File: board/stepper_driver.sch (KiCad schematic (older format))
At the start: 28 parts, among them J2301 CONN_STEPPER, J2302 CONN_2, U2301 L6470

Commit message: Worked a little on the PCB layout.
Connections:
- net at C2301.1, D2301.3 (cathode), U2301.14 (VBOOT): no longer C2302.1
- net at C2302.2, U2301.13 (CP): no longer D2301.2 (AK)
- new net: C2302.1, D2301.2 (AK)
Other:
- moved on the sheet: C2401, C2402, D2401
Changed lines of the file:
@@
 L +24V #PWR0185
 U 1 1 52E46E92
-P 6150 2000
+P 6000 2000
 AR Path="/52E6C2E8/52E46E92" Ref="#PWR0185"  Part="1"
 AR Path="/52FD6269/52E46E92" Ref="#PWR0216"  Part="1"
 AR Path="/52FD745B/52E46E92" Ref="#PWR0247"  Part="1"
 AR Path="/52FD7E0D/52E46E92" Ref="#PWR0278"  Part="1"
-F 0 "#PWR0216" H 6150 1950 20  0001 C CNN
-F 1 "+24V" H 6150 2100 30  0000 C CNN
-F 2 "" H 6150 2000 60  0000 C CNN
-F 3 "" H 6150 2000 60  0000 C CNN
-	1    6150 2000
+F 0 "#PWR0216" H 6000 1950 20  0001 C CNN
+F 1 "+24V" H 6000 2100 30  0000 C CNN
+F 2 "" H 6000 2000 60  0000 C CNN
+F 3 "" H 6000 2000 60  0000 C CNN
+	1    6000 2000
 	1    0    0    -1
 $EndComp
@@
 Text HLabel 4350 4750 0    60   Input ~ 0
 SCK
-Text HLabel 4350 4850 0    60   Input ~ 0
+Text HLabel 4350 4850 0    60   Output ~ 0
 SDO
 Text HLabel 4350 4950 0    60   Input ~ 0
@@
 L C C2301
 U 1 1 52E47AD8
-P 5700 2100
+P 5550 2100
 AR Path="/52E6C2E8/52E47AD8" Ref="C2301"  Part="1"
 AR Path="/52FD6269/52E47AD8" Ref="C2401"  Part="1"
 AR Path="/52FD745B/52E47AD8" Ref="C2501"  Part="1"
 AR Path="/52FD7E0D/52E47AD8" Ref="C2601"  Part="1"
-F 0 "C2401" H 5700 2200 40  0000 L CNN
-F 1 "220nF" H 5706 2015 40  0000 L CNN
-F 2 "" H 5738 1950 30  0000 C CNN
-F 3 "http://www.digikey.ca/product-detail/en/CL21B224KCFSFNE/1276-2949-1-ND/3891035" H 5700 2100 60  0001 C CNN
-F 4 "1276-2949-1-ND" H 6900 4550 60  0001 C CNN "Digikey Number"
-	1    5700 2100
+F 0 "C2401" H 5550 2200 40  0000 L CNN
+F 1 "220nF" H 5556 2015 40  0000 L CNN
+F 2 "" H 5588 1950 30  0000 C CNN
+F 3 "http://www.digikey.ca/product-detail/en/CL21B224KCFSFNE/1276-2949-1-ND/3891035" H 5550 2100 60  0001 C CNN
+F 4 "1276-2949-1-ND" H 6750 4550 60  0001 C CNN "Digikey Number"
+	1    5550 2100
 	0    -1   -1   0
 $EndComp
@@
 L C C2302
 U 1 1 52E47AE3
-P 5450 2700
+P 5550 2850
 AR Path="/52E6C2E8/52E47AE3" Ref="C2302"  Part="1"
 AR Path="/52FD6269/52E47AE3" Ref="C2402"  Part="1"
 AR Path="/52FD745B/52E47AE3" Ref="C2502"  Part="1"
 AR Path="/52FD7E0D/52E47AE3" Ref="C2602"  Part="1"
-F 0 "C2402" H 5450 2800 40  0000 L CNN
-F 1 "10nF" H 5456 2615 40  0000 L CNN
-F 2 "" H 5488 2550 30  0000 C CNN
-F 3 "http://www.digikey.ca/product-detail/en/C1608X7R2A103K080AA/445-1304-1-ND/567706" H 5450 2700 60  0001 C CNN
-F 4 "445-1304-1-ND" H 6900 4550 60  0001 C CNN "Digikey Number"
-	1    5450 2700
-	0    -1   -1   0
+F 0 "C2402" H 5550 2950 40  0000 L CNN
+F 1 "10nF" H 5556 2765 40  0000 L CNN
+F 2 "" H 5588 2700 30  0000 C CNN
+F 3 "http://www.digikey.ca/product-detail/en/C1608X7R2A103K080AA/445-1304-1-ND/567706" H 5550 2850 60  0001 C CNN
+F 4 "445-1304-1-ND" H 7000 4700 60  0001 C CNN "Digikey Number"
+	1    5550 2850
+	1    0    0    -1
 $EndComp
 $Comp
 L DOUBLE_SCHOTTKY D2301
 U 1 1 52F6EE9F
-P 5700 2350
+P 5550 2350
 AR Path="/52E6C2E8/52F6EE9F" Ref="D2301"  Part="1"
 AR Path="/52FD6269/52F6EE9F" Ref="D2401"  Part="1"
 AR Path="/52FD745B/52F6EE9F" Ref="D2501"  Part="1"
 AR Path="/52FD7E0D/52F6EE9F" Ref="D2601"  Part="1"
-F 0 "D2401" H 5800 2250 40  0000 C CNN
-F 1 "DOUBLE_SCHOTTKY" H 5700 2450 40  0001 C CNN
-F 2 "" H 5700 2350 60  0000 C CNN
-F 3 "http://www.digikey.ca/product-detail/en/BAS70-04-TP/BAS70-04TPMSCT-ND/717333" H 5700 2350 60  0001 C CNN
-F 4 "BAS70-04TPMSCT-ND" H 6900 4550 60  0001 C CNN "Digikey Number"
-	1    5700 2350
+F 0 "D2401" H 5650 2250 40  0000 C CNN
+F 1 "DOUBLE_SCHOTTKY" H 5550 2450 40  0001 C CNN
+F 2 "" H 5550 2350 60  0000 C CNN
+F 3 "http://www.digikey.ca/product-detail/en/BAS70-04-TP/BAS70-04TPMSCT-ND/717333" H 5550 2350 60  0001 C CNN
+F 4 "BAS70-04TPMSCT-ND" H 6750 4550 60  0001 C CNN "Digikey Number"
+	1    5550 2350
 	-1   0    0    -1
 $EndComp
@@
 	1    0    0    -1
 $EndComp
-Text HLabel 1800 4450 0    60   BiDi ~ 0
+Text HLabel 1800 4450 0    60   Input ~ 0
 ~STBY/RST
 $Comp
@@
 Text Notes 6700 2400 0    60   ~ 0
 1 per Corner
-Text Notes 5350 1800 0    60   ~ 0
+Text Notes 5200 1800 0    60   ~ 0
 Charge Pump
 Wire Wire Line
@@
 Connection ~ 5750 3250
 Wire Wire Line
-	5200 2700 5250 2700
-Wire Wire Line
-	5300 2350 5200 2350
-Connection ~ 5200 2350
-Connection ~ 5200 2700
-Connection ~ 6150 2100
-Wire Wire Line
-	6150 2350 6100 2350
-Wire Wire Line
-	6150 2000 6150 2350
-Wire Wire Line
-	5900 2100 6150 2100
-Wire Wire Line
-	5200 2100 5200 2950
-Wire Wire Line
-	5200 2100 5500 2100
-Wire Wire Line
-	5450 2950 5450 3350
-Wire Wire Line
-	5550 2950 5550 3350
+	5150 2350 5050 2350
+Connection ~ 5050 2350
+Connection ~ 6000 2100
+Wire Wire Line
+	6000 2350 5950 2350
+Wire Wire Line
+	6000 2000 6000 2350
+Wire Wire Line
+	5750 2100 6000 2100
+Wire Wire Line
+	5050 2100 5350 2100
 Wire Wire Line
 	5450 5750 5450 5850
@@
 Wire Wire Line
 	3850 3100 3850 3200
-Wire Wire Line
-	5700 2550 5700 2950
-Wire Wire Line
-	5650 2700 5700 2700
-Connection ~ 5700 2700
-Wire Wire Line
-	5200 2950 5450 2950
-Wire Wire Line
-	5700 2950 5550 2950
 Wire Wire Line
 	6550 3850 6650 3850
@@
 	1    0    0    -1
 $EndComp
+Wire Wire Line
+	5050 2100 5050 3000
+Wire Wire Line
+	5050 3000 5450 3000
+Wire Wire Line
+	5450 3000 5450 3350
+Wire Wire Line
+	5550 3350 5550 3050
+Wire Wire Line
+	5550 2650 5550 2550
 $EndSCHEMATC

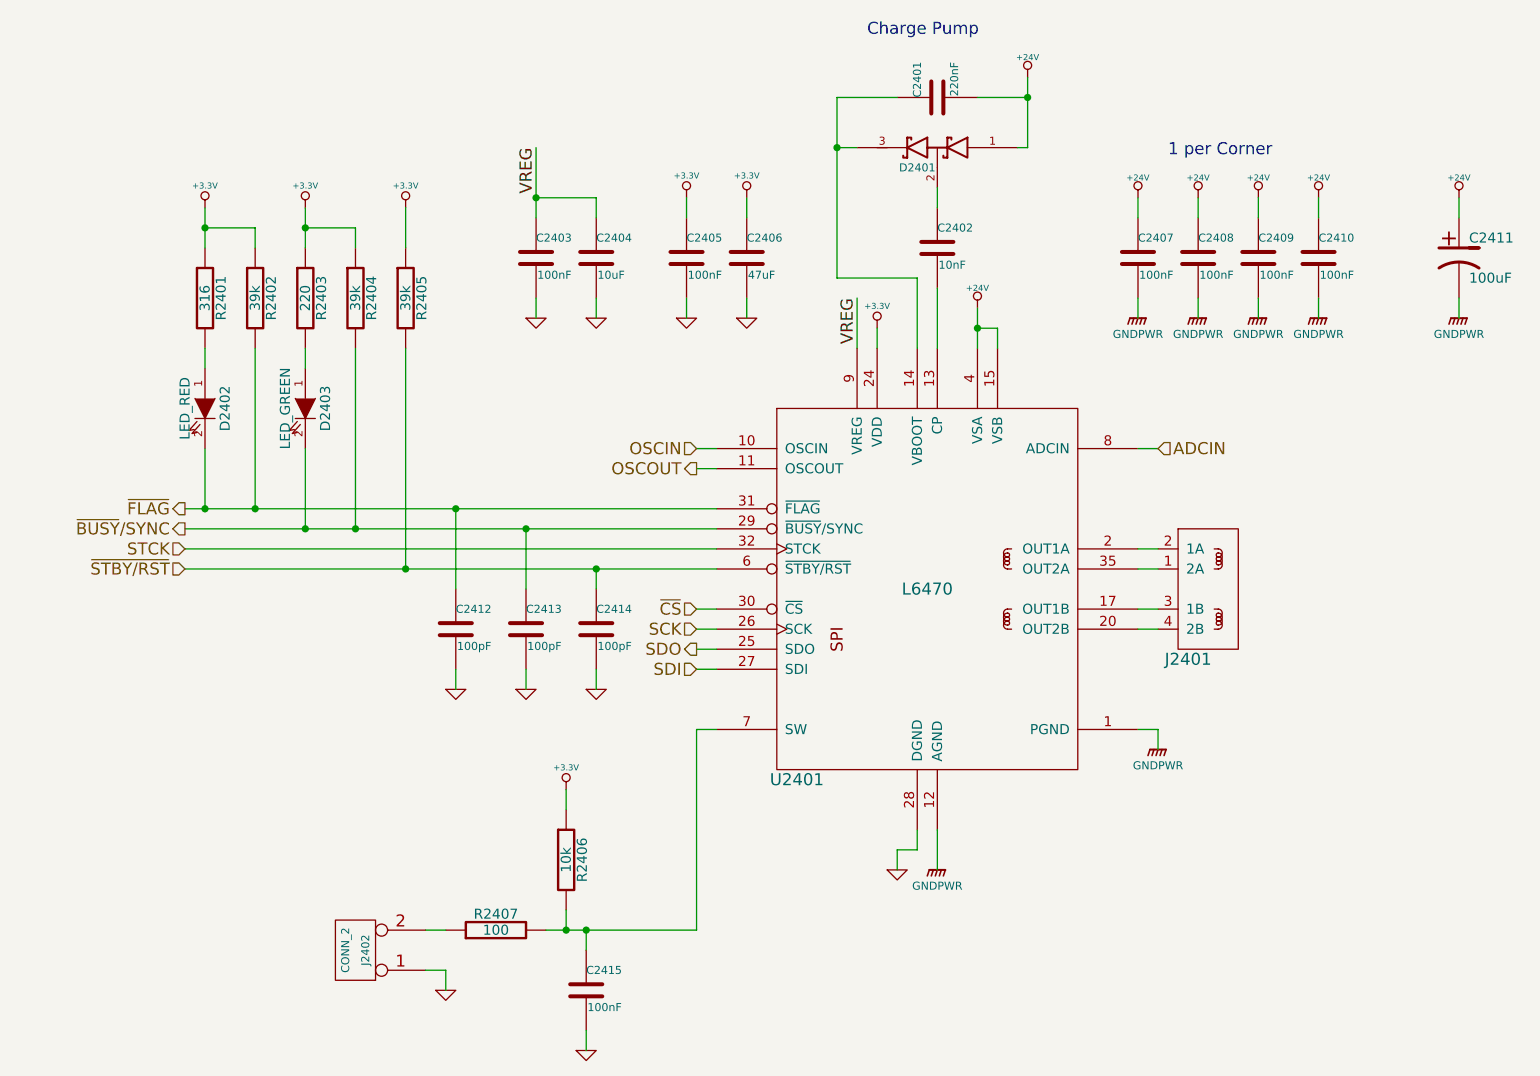
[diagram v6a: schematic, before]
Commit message: Removed PWR-GND, change footprint for a bunch of capacitors
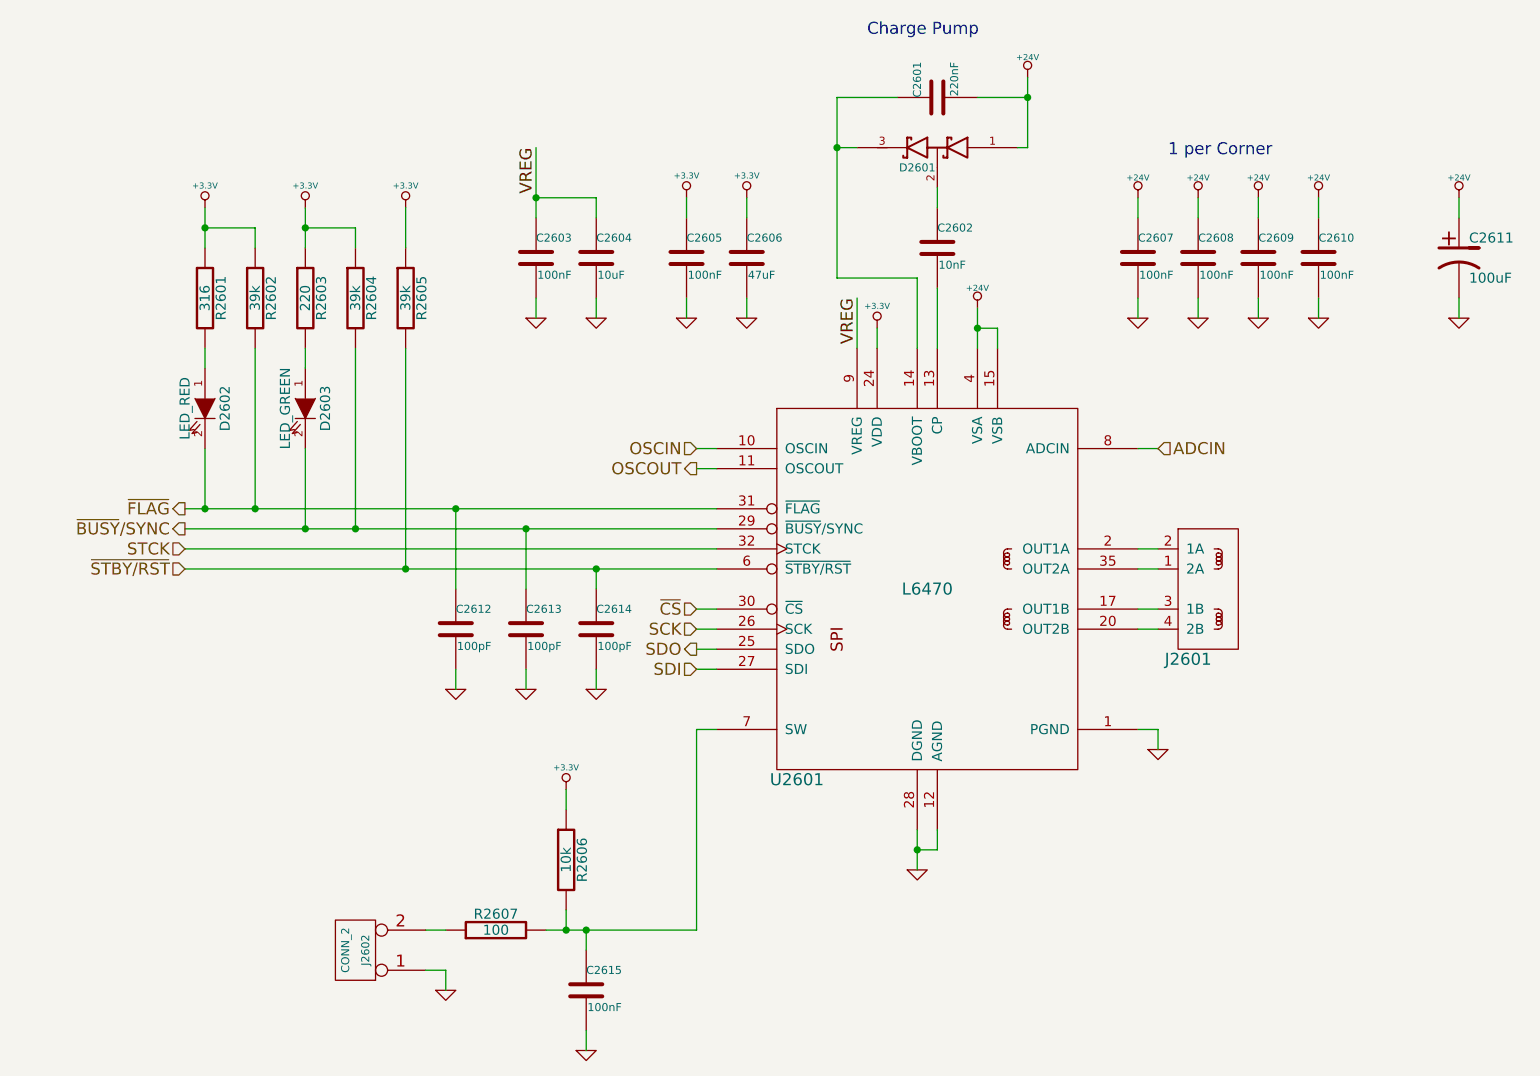
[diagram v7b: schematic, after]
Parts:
- C2307, C2308, C2309, C2310: Digikey Number 445-6938-1-ND -> 399-6753-1-ND
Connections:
- net GNDPWR is gone; now on net GND: C2307.2, C2308.2, C2309.2, C2310.2, C2311.2, U2301.1 (PGND), U2301.12 (AGND), U2301.19 (PGND), U2301.PAD (PGND)
